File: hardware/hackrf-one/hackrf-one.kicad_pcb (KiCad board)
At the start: 4 copper layers, 120 x 75 mm, 432 parts, among them J1 USB-MICRO-B, J10 GND_CLIP, J2 RF-SHIELD-FRAME, J3 RF-SHIELD-COVER, J4 MOUNTING_HOLE, J5 MOUNTING_HOLE, J6 MOUNTING_HOLE, J7 MOUNTING_HOLE, J8 MOUNTING_HOLE, J9 MOUNTING_HOLE, P1 1V8, P13 GPO1, P14 XCVR_CLKOUT, P15 INTR, P16 CLKIN, P17 GPO6, P18 OEB, P19 GPO3, P2 CLKOUT, P20 GPIO, P21 REF_IN, P22 I2S, P23 DBGEN, P24 TRST, P25 LPC_ISP, P26 LPC_JTAG, P27 MIXER_SDATA, P28 SD, P29 CPLD_JTAG, P3 GND, P30 BANK2_AUX, P31 MIXER_SCLK, P32 MIXER_ENX, P33 MIXER_RESETX, P34 MIX_BYPASS, P35 !MIX_BYPASS, P36 VAA, P37 SCL, P38 SDA, P39 SSP1_SCK, P4 ANTENNA, P40 SSP1_MOSI, P41 SSP1_MISO, P42 TX, P43 RX, P44 HP, P45 LP, P46 TX_MIX_BP, P47 RX_MIX_BP, P48 TX_AMP, P49 RX_AMP, P5 LEDS, P50 AMP_BYPASS, P51 !TX_AMP_PWR, P52 !RX_AMP_PWR, P53 CS_XCVR, P54 CS_AD, P55 TXENABLE, P56 RXENABLE, P57 XTAL2, P58 GCK1, P59 GCK2, P6 GPO4, P60 SGPIO_CLK, P61 DA0, P62 DA7, P63 DD0, P64 DD9, P65 DA4, P66 DD5, P67 RSSI, P68 SPIFI_CS, P69 VREGMODE, P7 GPO2, P70 EN_1V8, P71 ID, P72 GP_CLKIN, P73 P1_2, P74 P1_1, P75 GP_CLKIN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

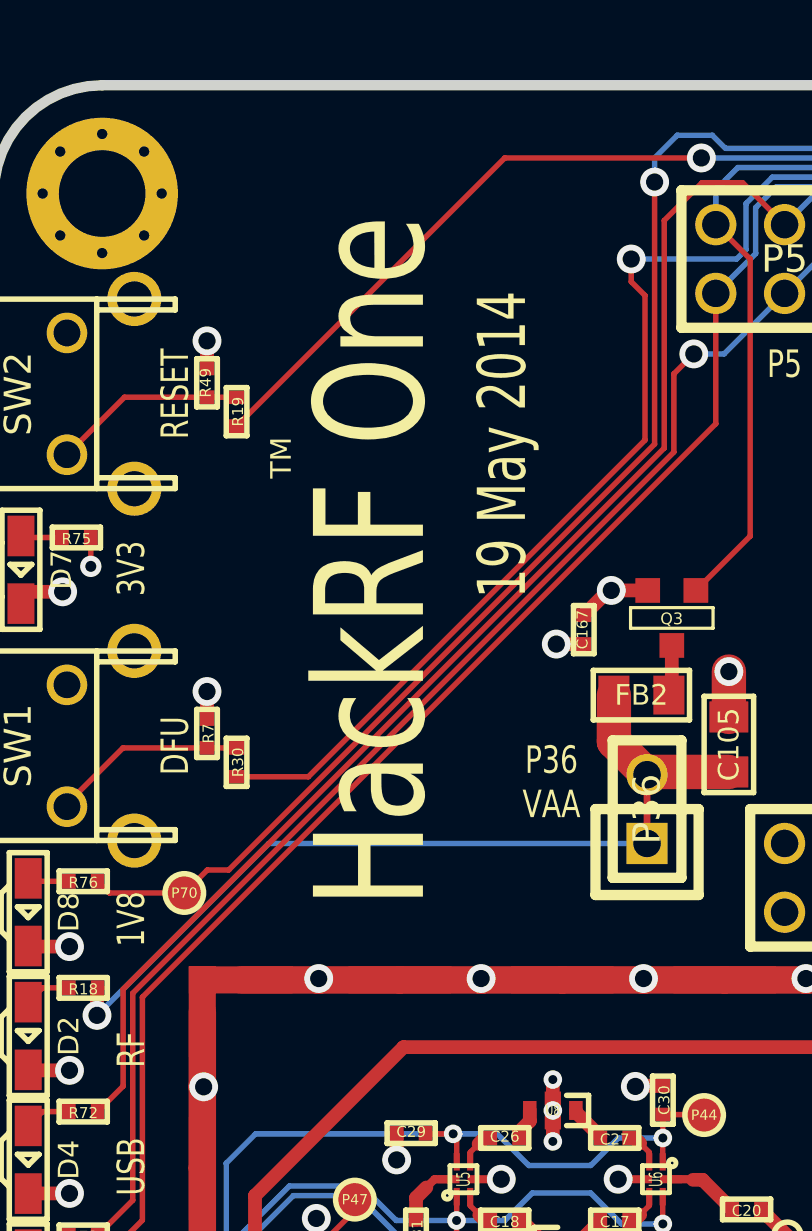
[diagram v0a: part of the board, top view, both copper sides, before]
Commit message: additional small silk tweak
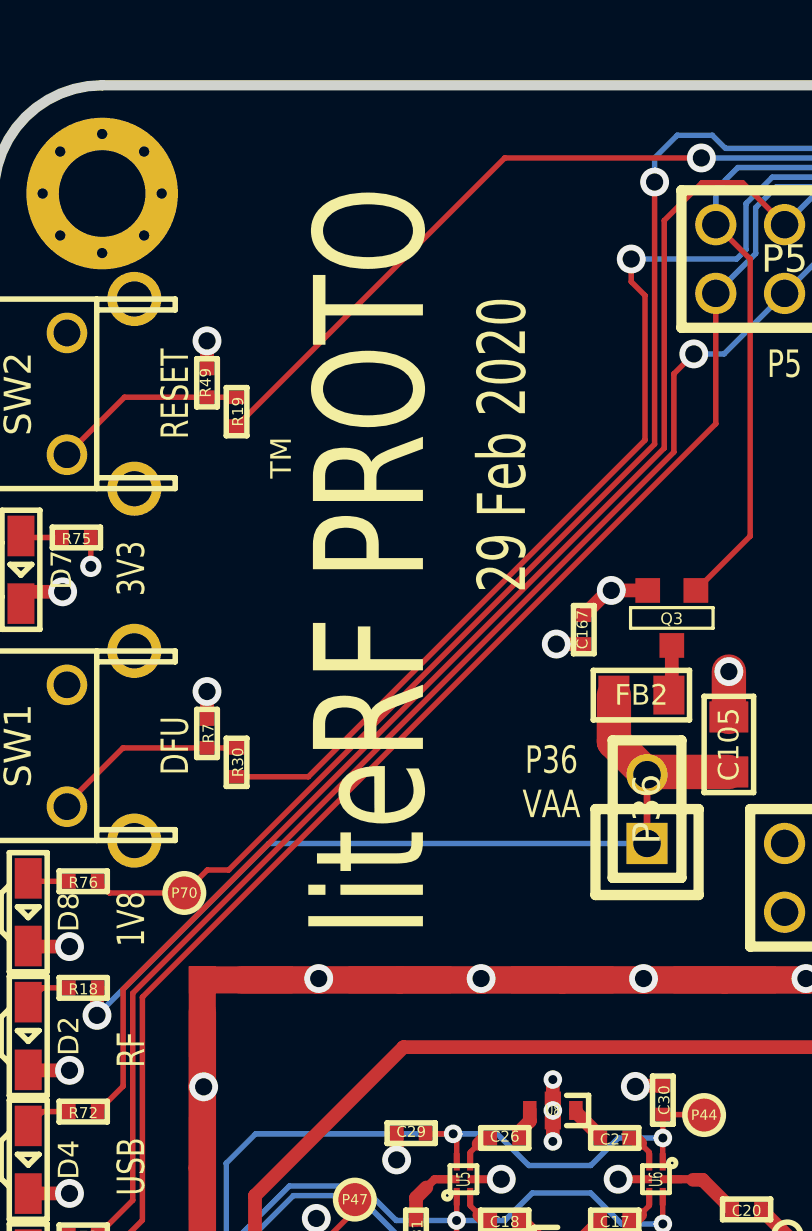
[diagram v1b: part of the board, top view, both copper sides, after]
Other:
- board text added: "29 Feb 2020"
- board text added: "liteRF PROTO"
- board text removed: "19 May 2014"
- board text removed: "HackRF One"
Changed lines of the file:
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@@
     (effects (font (size 1.016 1.016) (thickness 0.1778)))
   )
-  (gr_text "19 May 2014" (at 78.796 113.278 90) (layer F.SilkS)
+  (gr_text "29 Feb 2020" (at 78.796 113.278 90) (layer F.SilkS)
     (effects (font (size 1.778 1.27) (thickness 0.3048)))
   )
@@
     (effects (font (size 1.016 0.762) (thickness 0.1905)))
   )
-  (gr_text "HackRF One" (at 73.97 117.596 90) (layer F.SilkS)
+  (gr_text "liteRF PROTO" (at 73.97 117.596 90) (layer F.SilkS)
     (effects (font (size 4.064 3.048) (thickness 0.6096)))
   )
